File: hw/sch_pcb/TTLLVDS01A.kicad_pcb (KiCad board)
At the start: 2 copper layers, 40.1 x 19.8 mm, 17 parts, among them J1 JUMP_3X2, J2 HEADER_2x01_PARALLEL, J3 HEADER_2x01_PARALLEL, J4 HEADER_2x01_PARALLEL, J5 HEADER_2x01_PARALLEL, J6 SATA7-67491-1030, M1 HOLE, M2 HOLE, M3 HOLE, M4 HOLE, U1 SN65LVDS9638D

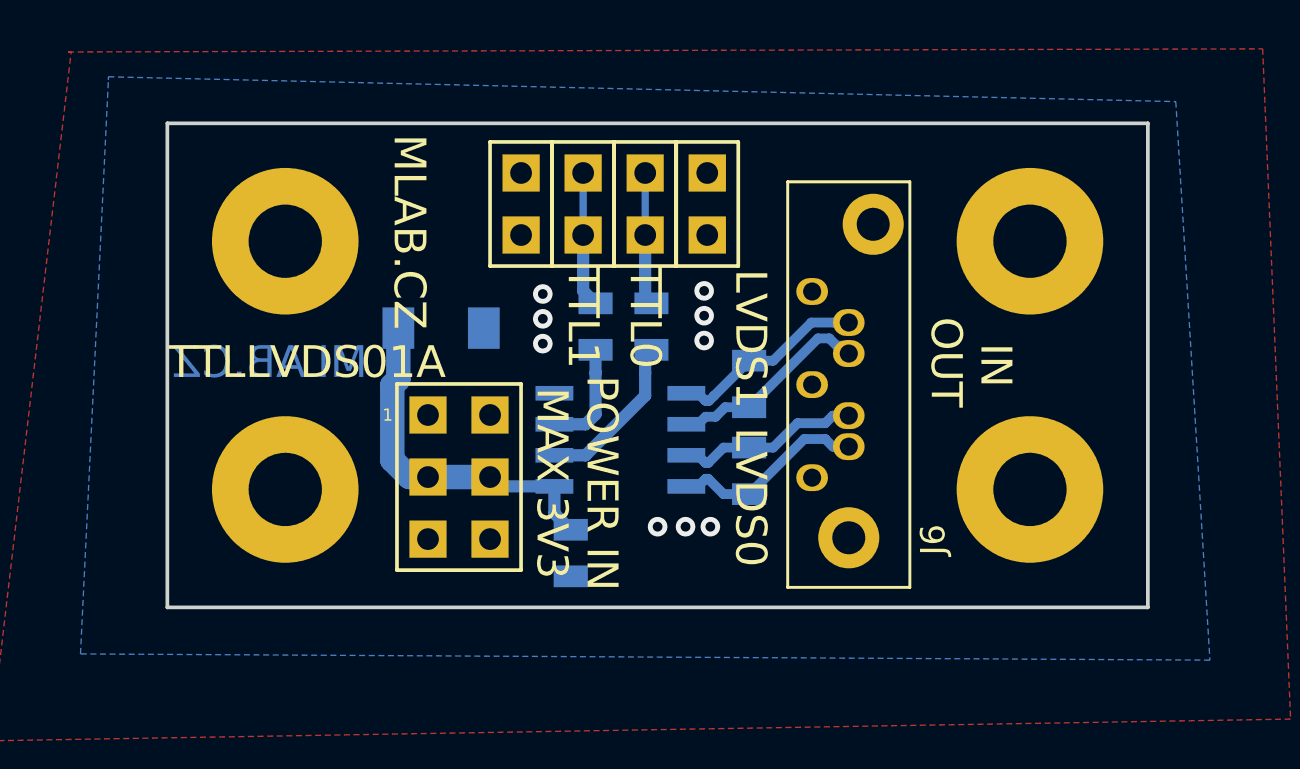
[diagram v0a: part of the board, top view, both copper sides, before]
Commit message: Update project to KiCAD 6.0. Update PCB silkscreen.
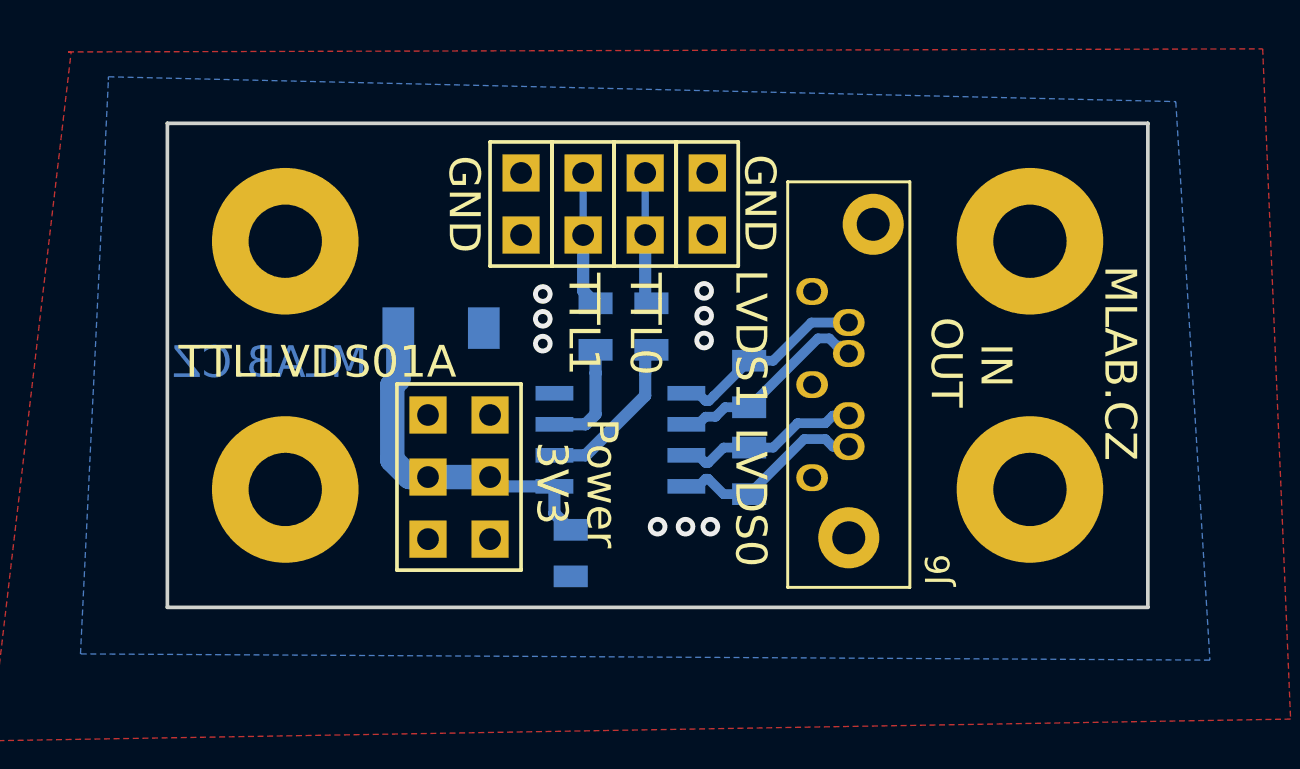
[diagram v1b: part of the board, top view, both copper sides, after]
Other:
- net class Default removed
- net class MLAB_power removed
- board text added: "GND"
- board text added: "Power 3V3"
- board text removed: "POWER IN MAX 3V3"

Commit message: Update documentation.
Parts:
- moved C2 171.2 mm to (142.8, 113.3)
- moved J2 171.2 mm to (145.9, 99.0)
- moved M2 171.2 mm to (131.2, 110.7)
- moved R3 171.2 mm to (150.2, 109.9)
- moved R4 171.2 mm to (150.2, 106.4)
- moved D1 171.2 mm to (137.5, 104.1)
- moved J1 171.2 mm to (138.3, 110.2)
- moved J3 171.2 mm to (140.8, 99.0)
- moved J4 171.2 mm to (143.4, 99.0)
- moved J5 171.2 mm to (148.4, 99.0)
- moved J6 171.2 mm to (152.7, 110.2)
- moved M1 171.2 mm to (161.6, 100.5)
- moved M3 171.2 mm to (131.2, 100.5)
- moved M4 171.2 mm to (161.6, 110.7)
- moved R1 171.2 mm to (146.2, 104.0)
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
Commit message: Zmena pouzder na nova KiCAD a poslední kontroly pred vyrobou
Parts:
- C2, R1, R2: footprint Mlab_R:SMD-0805 -> Resistor_SMD:R_0805_2012Metric
- R3, R4: value 100R -> 100; footprint Mlab_R:SMD-0805 -> Resistor_SMD:R_0805_2012Metric
